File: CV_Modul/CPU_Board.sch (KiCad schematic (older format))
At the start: 122 parts, among them J101 Screw_Terminal_01x03, J102 Conn_02x01, J103 Conn_02x01, J104 Conn_01x08_Male, J105 Conn_02x09_Odd_Even, J106 Micro_SD_Card_Det, J107 Conn_01x06_Male, J108 Conn_02x01, J109 Conn_02x01, J110 Screw_Terminal_01x04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

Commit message: CV Modul Reset Button hinzugefügt
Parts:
- added SW102: SW_Push, ProjectFootprints:TactileSwitchLCSC, symbol Switch:SW_Push
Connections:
- net GND: now also SW102.1
- net NRST: now also SW102.2
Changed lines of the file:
@@
 Wire Wire Line
 	2000 2300 2000 2250
-Wire Wire Line
-	1700 2300 2000 2300
 Connection ~ 2000 2300
 Text Label 1700 2300 2    50   ~ 0
@@
 Text Notes 11450 6700 0    50   ~ 0
 IDC Connector for BOM\n16P 2Rows 2,54mm Pitch
+$Comp
+L Switch:SW_Push SW102
+U 1 1 6033743F
+P 1150 2300
+F 0 "SW102" H 1150 2585 50  0000 C CNN
+F 1 "SW_Push" H 1150 2494 50  0000 C CNN
+F 2 "ProjectFootprints:TactileSwitchLCSC" H 1150 2500 50  0001 C CNN
+F 3 "" H 1150 2500 50  0001 C CNN
+F 4 "C455137" H -1750 -3550 50  0001 C CNN "LCSC"
+	1    1150 2300
+	1    0    0    -1
+$EndComp
+Wire Wire Line
+	1350 2300 2000 2300
+$Comp
+L power:GND #PWR?
+U 1 1 603B1885
+P 950 2300
+AR Path="/5FDD0F66/603B1885" Ref="#PWR?"  Part="1"
+AR Path="/603B1885" Ref="#PWR0169"  Part="1"
+F 0 "#PWR0169" H 950 2050 50  0001 C CNN
+F 1 "GND" V 1050 2200 50  0000 R CNN
+F 2 "" H 950 2300 50  0001 C CNN
+F 3 "" H 950 2300 50  0001 C CNN
+	1    950  2300
+	0    1    1    0
+$EndComp
 $EndSCHEMATC

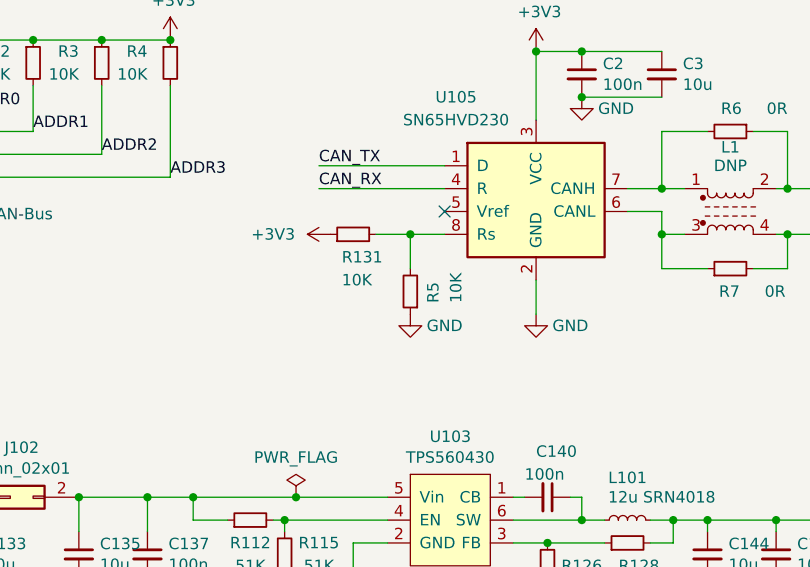
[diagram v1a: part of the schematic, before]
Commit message: CV Modul Strong 1K Pulldown CAN Phy für Fast Mode. STEP Modelle hinzugefügt. Connector für Kamera etwas nach rechts verschoben
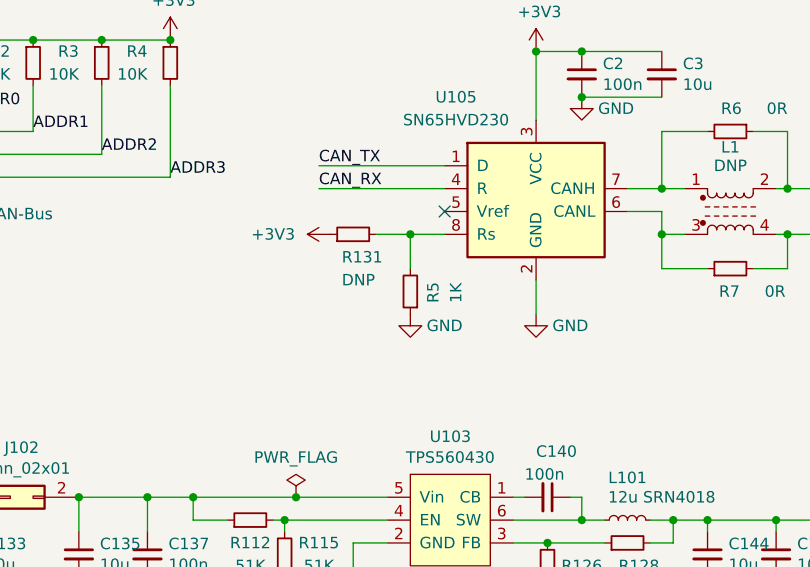
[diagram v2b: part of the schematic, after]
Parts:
- R131: value 10K -> DNP; LCSC C99198 -> 0
- R5: value 10K -> 1K; LCSC C99198 -> C14676
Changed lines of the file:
@@
 AR Path="/60391C5F" Ref="R5"  Part="1"
 F 0 "R5" V 12600 1850 50  0000 R CNN
-F 1 "10K" V 12500 1850 50  0000 R CNN
+F 1 "1K" V 12500 1850 50  0000 R CNN
 F 2 "Resistor_SMD:R_0603_1608Metric" H 12700 1800 50  0001 C CNN
 F 3 "~" H 12700 1800 50  0001 C CNN
-F 4 "C99198" H 12700 1800 50  0001 C CNN "LCSC"
+F 4 "C14676" H 12700 1800 50  0001 C CNN "LCSC"
 	1    12700 1800
 	-1   0    0    1
@@
 AR Path="/605A64FD" Ref="R131"  Part="1"
 F 0 "R131" V 12350 1600 50  0000 R CNN
-F 1 "10K" V 12250 1600 50  0000 R CNN
+F 1 "DNP" V 12250 1600 50  0000 R CNN
 F 2 "Resistor_SMD:R_0603_1608Metric" H 12450 1550 50  0001 C CNN
 F 3 "~" H 12450 1550 50  0001 C CNN
-F 4 "C99198" H 12450 1550 50  0001 C CNN "LCSC"
+F 4 "0" H 12450 1550 50  0001 C CNN "LCSC"
 	1    12450 1550
 	0    -1   -1   0

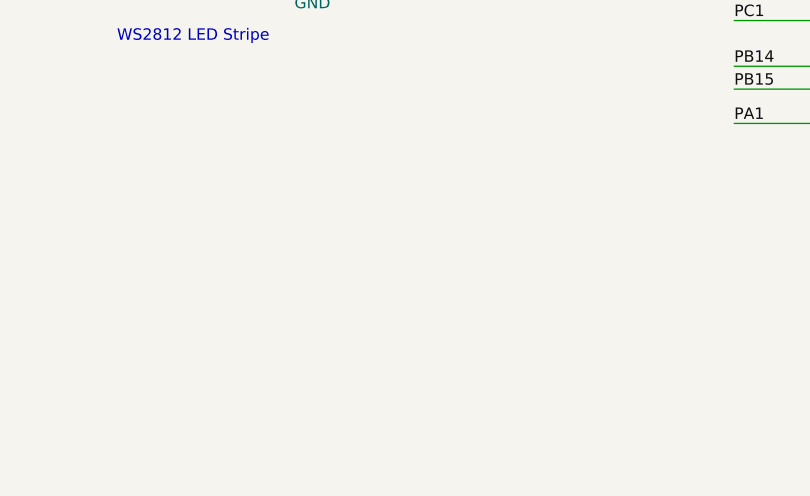
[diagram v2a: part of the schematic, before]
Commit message: Fiducials auf allen Boards hinzugefügt
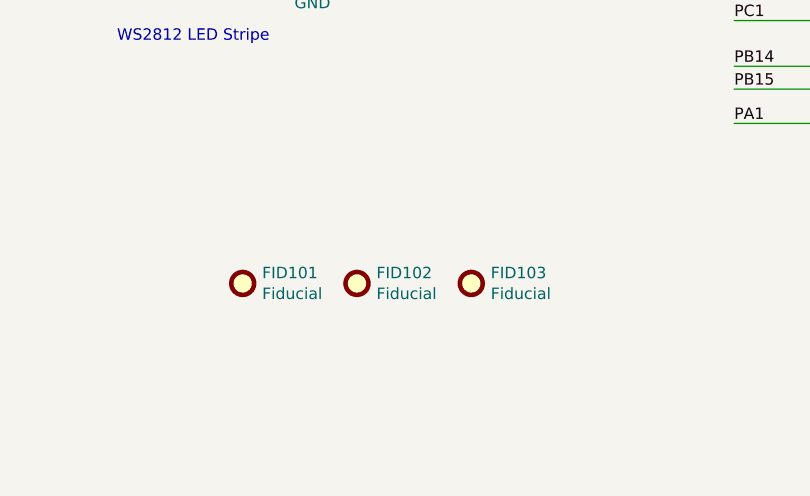
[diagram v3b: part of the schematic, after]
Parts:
- added FID101, FID102, FID103: Fiducial, Fiducial:Fiducial_1mm_Mask2mm, symbol Mechanical:Fiducial
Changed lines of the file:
@@
 	0    1    1    0
 $EndComp
+$Comp
+L Mechanical:Fiducial FID101
+U 1 1 6029B861
+P 10000 10000
+F 0 "FID101" H 10085 10046 50  0000 L CNN
+F 1 "Fiducial" H 10085 9955 50  0000 L CNN
+F 2 "Fiducial:Fiducial_1mm_Mask2mm" H 10000 10000 50  0001 C CNN
+F 3 "~" H 10000 10000 50  0001 C CNN
+	1    10000 10000
+	1    0    0    -1
+$EndComp
+$Comp
+L Mechanical:Fiducial FID102
+U 1 1 602A2CB7
+P 10500 10000
+F 0 "FID102" H 10585 10046 50  0000 L CNN
+F 1 "Fiducial" H 10585 9955 50  0000 L CNN
+F 2 "Fiducial:Fiducial_1mm_Mask2mm" H 10500 10000 50  0001 C CNN
+F 3 "~" H 10500 10000 50  0001 C CNN
+	1    10500 10000
+	1    0    0    -1
+$EndComp
+$Comp
+L Mechanical:Fiducial FID103
+U 1 1 602A329F
+P 11000 10000
+F 0 "FID103" H 11085 10046 50  0000 L CNN
+F 1 "Fiducial" H 11085 9955 50  0000 L CNN
+F 2 "Fiducial:Fiducial_1mm_Mask2mm" H 11000 10000 50  0001 C CNN
+F 3 "~" H 11000 10000 50  0001 C CNN
+	1    11000 10000
+	1    0    0    -1
+$EndComp
 $EndSCHEMATC

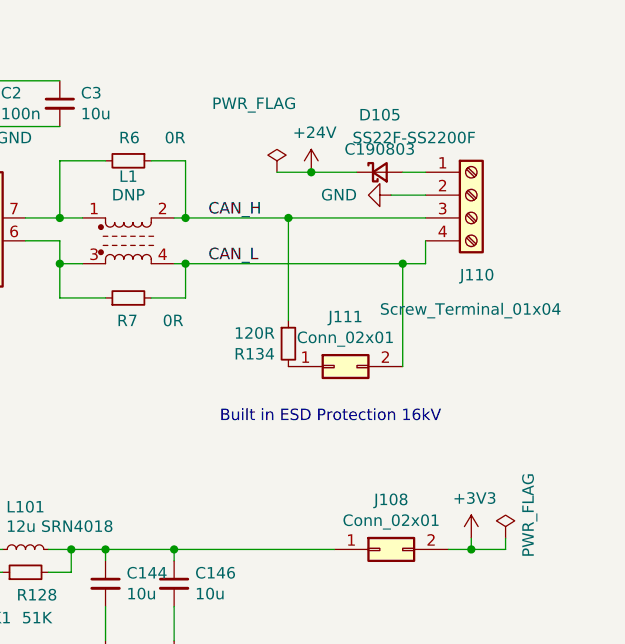
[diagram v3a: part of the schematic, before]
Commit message: ESD Protection überarbeitet, aber noch nicht fertig
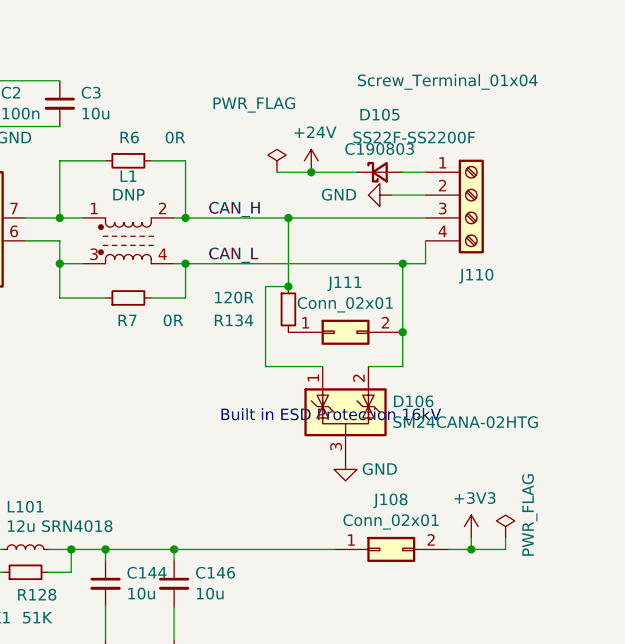
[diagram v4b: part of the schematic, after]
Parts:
- added D106: SM24CANA-02HTG, Package_TO_SOT_SMD:SOT-23, symbol Power_Protection:NUP2105L
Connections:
- net CAN_H: now also D106.1 (K)
- net CAN_L: now also D106.2 (K)
- net GND: now also D106.3 (A)
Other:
- moved on the sheet: J111, R134
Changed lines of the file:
@@
 AR Path="/6005408A" Ref="J110"  Part="1"
 F 0 "J110" H 15550 900 50  0000 L CNN
-F 1 "Screw_Terminal_01x04" H 15200 750 50  0000 L CNN
+F 1 "Screw_Terminal_01x04" H 15100 1750 50  0000 L CNN
 F 2 "TerminalBlock_RND:TerminalBlock_RND_205-00047_1x04_P5.00mm_Horizontal" H 15600 1250 50  0001 C CNN
 F 3 "~" H 15600 1250 50  0001 C CNN
@@
 L Device:R_Small R?
 U 1 1 601B485F
-P 14800 1900
+P 14800 1750
 AR Path="/5FDD0F66/601B485F" Ref="R?"  Part="1"
 AR Path="/601B485F" Ref="R134"  Part="1"
-F 0 "R134" H 14741 1854 50  0000 R CNN
-F 1 "120R" H 14741 1945 50  0000 R CNN
-F 2 "Resistor_SMD:R_0603_1608Metric" H 14800 1900 50  0001 C CNN
-F 3 "~" H 14800 1900 50  0001 C CNN
-F 4 "C114681" H 14800 1900 50  0001 C CNN "LCSC"
-	1    14800 1900
+F 0 "R134" H 14650 1700 50  0000 R CNN
+F 1 "120R" H 14650 1800 50  0000 R CNN
+F 2 "Resistor_SMD:R_0603_1608Metric" H 14800 1750 50  0001 C CNN
+F 3 "~" H 14800 1750 50  0001 C CNN
+F 4 "C114681" H 14800 1750 50  0001 C CNN "LCSC"
+	1    14800 1750
 	1    0    0    -1
 $EndComp
@@
 L Connector_Generic:Conn_02x01 J?
 U 1 1 601B48C8
-P 15000 2000
+P 15000 1850
 AR Path="/5EA6895E/601B48C8" Ref="J?"  Part="1"
 AR Path="/5ED2496F/601B48C8" Ref="J?"  Part="1"
 AR Path="/601B48C8" Ref="J111"  Part="1"
 AR Path="/5FDD0F66/601B48C8" Ref="J?"  Part="1"
-F 0 "J111" H 15050 2217 50  0000 C CNN
-F 1 "Conn_02x01" H 15050 2126 50  0000 C CNN
-F 2 "Connector_PinHeader_2.54mm:PinHeader_1x02_P2.54mm_Vertical" H 15000 2000 50  0001 C CNN
-F 3 "~" H 15000 2000 50  0001 C CNN
-F 4 "0" H 15000 2000 50  0001 C CNN "LCSC"
-	1    15000 2000
+F 0 "J111" H 15050 2067 50  0000 C CNN
+F 1 "Conn_02x01" H 15050 1976 50  0000 C CNN
+F 2 "Connector_PinHeader_2.54mm:PinHeader_1x02_P2.54mm_Vertical" H 15000 1850 50  0001 C CNN
+F 3 "~" H 15000 1850 50  0001 C CNN
+F 4 "0" H 15000 1850 50  0001 C CNN "LCSC"
+	1    15000 1850
 	1    0    0    -1
 $EndComp
@@
 	14350 1550 15300 1550
 Wire Wire Line
-	14800 1800 14800 1350
+	14800 1650 14800 1350
 Connection ~ 14800 1350
 Wire Wire Line
 	14800 1350 15400 1350
 Wire Wire Line
-	15300 2000 15300 1550
+	15300 1850 15300 1550
 Connection ~ 15300 1550
 Wire Wire Line
@@
 	1    0    0    -1
 $EndComp
+$Comp
+L Power_Protection:NUP2105L D106
+U 1 1 6051675A
+P 15050 2200
+F 0 "D106" H 15255 2246 50  0000 L CNN
+F 1 "SM24CANA-02HTG" H 15255 2155 50  0000 L CNN
+F 2 "Package_TO_SOT_SMD:SOT-23" H 15275 2150 50  0001 L CNN
+F 3 "http://www.onsemi.com/pub_link/Collateral/NUP2105L-D.PDF" H 15175 2325 50  0001 C CNN
+F 4 "C151236" H 15050 2200 50  0001 C CNN "LCSC"
+	1    15050 2200
+	1    0    0    -1
+$EndComp
+Wire Wire Line
+	15150 2000 15300 2000
+Wire Wire Line
+	15300 2000 15300 1850
+Connection ~ 15300 1850
+Wire Wire Line
+	14800 1650 14700 1650
+Wire Wire Line
+	14700 1650 14700 2000
+Wire Wire Line
+	14700 2000 14950 2000
+Connection ~ 14800 1650
+$Comp
+L power:GND #PWR?
+U 1 1 605D6839
+P 15050 2400
+AR Path="/5FDD0F66/605D6839" Ref="#PWR?"  Part="1"
+AR Path="/605D6839" Ref="#PWR0170"  Part="1"
+F 0 "#PWR0170" H 15050 2150 50  0001 C CNN
+F 1 "GND" H 15200 2350 50  0000 C CNN
+F 2 "" H 15050 2400 50  0001 C CNN
+F 3 "" H 15050 2400 50  0001 C CNN
+	1    15050 2400
+	1    0    0    -1
+$EndComp

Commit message: Änderungen für bestellung V01 -  Bestellung abgeschickt
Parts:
- FID101, FID102, FID103: LCSC (none) -> 0
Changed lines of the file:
@@
 F 2 "Fiducial:Fiducial_1mm_Mask2mm" H 10000 10000 50  0001 C CNN
 F 3 "~" H 10000 10000 50  0001 C CNN
+F 4 "0" H 10000 10000 50  0001 C CNN "LCSC"
 	1    10000 10000
 	1    0    0    -1
@@
 F 2 "Fiducial:Fiducial_1mm_Mask2mm" H 10500 10000 50  0001 C CNN
 F 3 "~" H 10500 10000 50  0001 C CNN
+F 4 "0" H 10500 10000 50  0001 C CNN "LCSC"
 	1    10500 10000
 	1    0    0    -1
@@
 F 2 "Fiducial:Fiducial_1mm_Mask2mm" H 11000 10000 50  0001 C CNN
 F 3 "~" H 11000 10000 50  0001 C CNN
+F 4 "0" H 11000 10000 50  0001 C CNN "LCSC"
 	1    11000 10000
 	1    0    0    -1

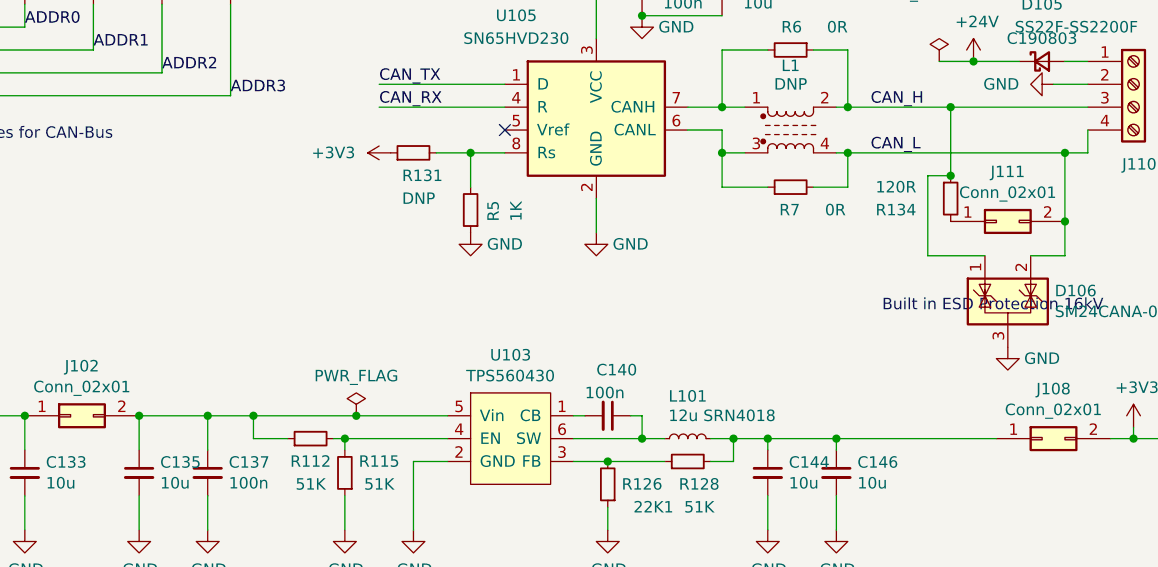
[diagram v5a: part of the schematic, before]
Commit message: Kleine Bugs im Feeder behoben, Löcher für Lagerhalter hinzugefügt
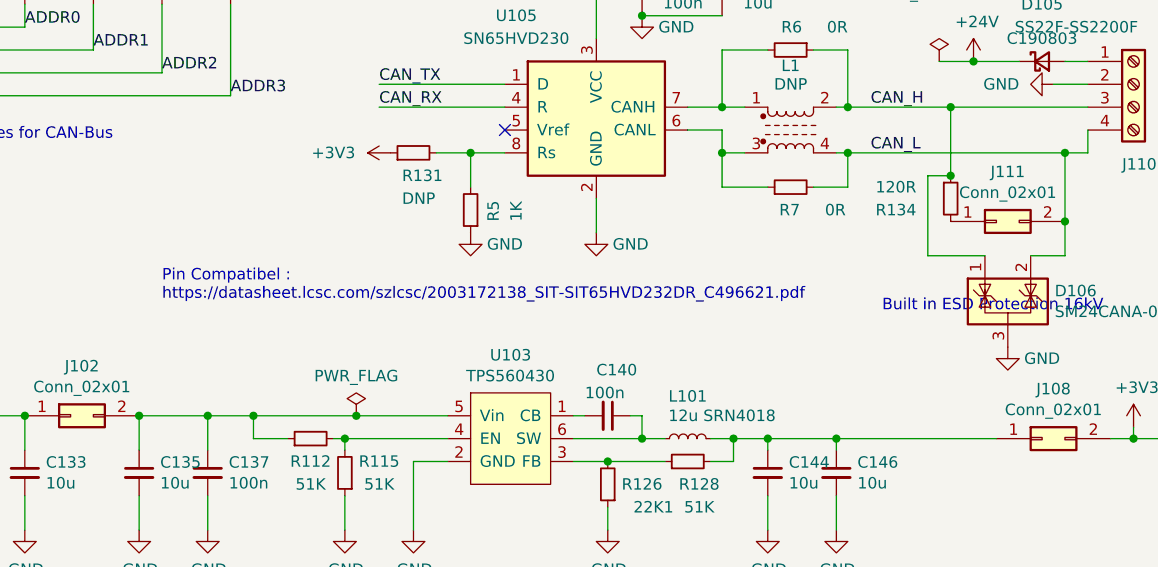
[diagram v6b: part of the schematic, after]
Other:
- note added: "Pin Compatibel :\nhttps://datasheet.lcsc.com/szlcsc/2003172138_SIT-SIT65HVD232DR_C496621.pdf"
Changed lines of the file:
@@
 	1    0    0    -1
 $EndComp
+Text Notes 11350 2200 0    50   ~ 0
+Pin Compatibel :\nhttps://datasheet.lcsc.com/szlcsc/2003172138_SIT-SIT65HVD232DR_C496621.pdf
 $EndSCHEMATC
